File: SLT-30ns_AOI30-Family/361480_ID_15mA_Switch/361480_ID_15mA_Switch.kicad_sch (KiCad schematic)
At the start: 7 parts, among them T1 ABA, T2 ABA, U1 12-Pin_SLx_Can

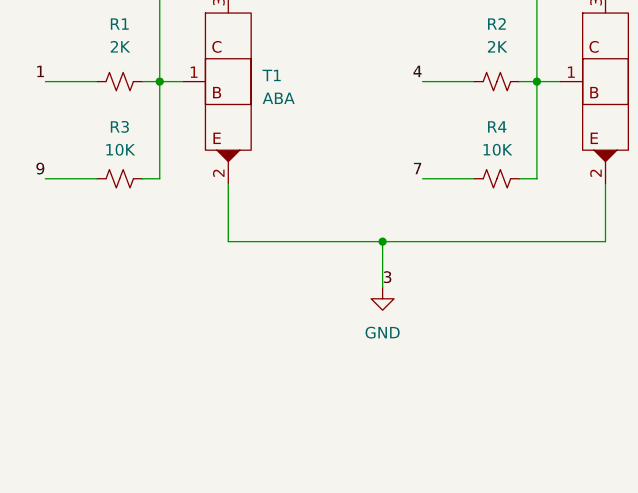
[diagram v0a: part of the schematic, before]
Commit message: Update schematic pdfs
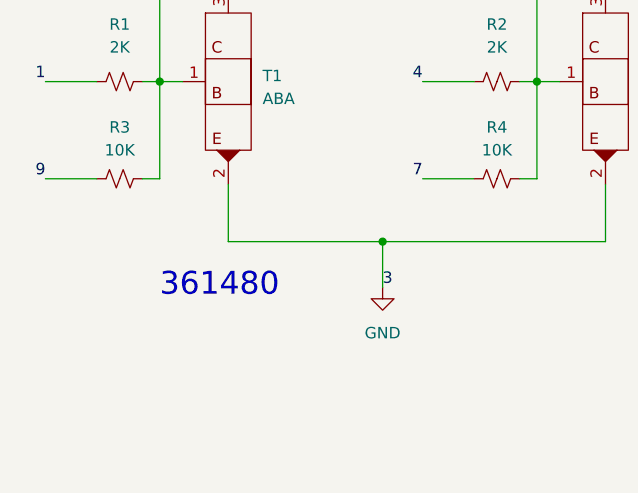
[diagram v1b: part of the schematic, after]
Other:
- note added: "361480"
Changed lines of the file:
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@@
     (stroke (width 0) (type default) (color 0 0 0 0))
+  )
+  (text "361480" (at 92.71 128.27 0)
+    (effects (font (size 2.54 2.54)) (justify left bottom))
   )
   (label "8" (at 142.24 85.725 0)
